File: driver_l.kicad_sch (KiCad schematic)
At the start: 0 parts

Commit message: Simplified sheet tree; fixed all labels
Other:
- company: (none) -> CC0-1.0 License
- title: (none) -> Left Driver
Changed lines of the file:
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@@
 	(generator_version "8.0")
 	(paper "A4")
+	(title_block
+		(title "Left Driver")
+		(date "2025-02-10")
+		(rev "INDEV")
+		(company "CC0-1.0 License")
+	)
 )

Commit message: Update driver motor scheme
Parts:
- added C10, C11, C12, C13, C14, C15, C16, C17, C20: ~, symbol Device:C
- added M1: Motor_DC, symbol Motor:Motor_DC
- added Q2: PNP, symbol Simulation_SPICE:PNP
- added Q5, Q6, Q7, Q8: IRFZ48N, symbol Pioneer:IRFZ48N
- added R2, R36, R63: 0, symbol Device:R
- added R26, R34, R38: ~, symbol Device:R
- added R27, R28, R29, R30: 200, symbol Device:R
- added R31, R32: 10.9k, symbol Device:R
- added R33: 5.62k, symbol Device:R
- added R35, R37, R41: 10k, symbol Device:R
- added R39: 27.4k, symbol Device:R
- added R40: 13.3k, symbol Device:R
- added R7, R8: 4.72k, symbol Device:R
- added U12, U6A, U6B: TS922I, symbol Device:Opamp_Dual
- added U13: TD340I, symbol Pioneer:TD340I
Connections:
- new net: C15.1, R34.1, R35.2, U6A.2 (-)
- new net: C15.2, R34.2, R37.1, U6A.1
- new net: C14.1, R39.1, R41.1, U12.8 (V+), U13.2 (VOUT)
- new net: C16.1, R36.1, U6A.3 (+)
- new net: R38.1, R39.2, R40.2, U6B.5 (+)
- new net: Q2.2 (B), R38.2, U6B.7
- new net: Q7.3 (S), R2.1, R26.1, R36.2
- new net: C17.1, R37.2, U6B.6 (-)
- new net: Q6.1 (G), R29.2
- new net: C10.2, Q6.2 (D)
- new net: C11.1, U13.16 (CB2)
- new net: C12.1, U13.19 (CB1)
- new net: R33.2, U13.20 (OSC)
- new net: R41.2, U13.6 (~{STBY})
- new net: Q2.1 (C), R7.2, U13.8 (IN1)
- new net: Q2.3 (E), R8.2, U13.9 (IN2)
- new net: Q8.1 (G), R27.2
- new net: Q7.1 (G), R30.2
- new net: C20.2, Q5.2 (D)
- new net: Q5.1 (G), R28.2
- new net +BATT: C10.1, C13.1, C20.1, U13.1 (VBATT)
- new net G1: U13.10 (CF), U13.4 (CWD)
- new net GND: C13.2, C14.2, C16.2, C17.2, Q8.3 (S), R2.2, R26.2, R31.2, R32.2, R33.1, R35.1, R40.1, R63.1, R63.2, U12.4 (V-), U13.11 (GND)
- new net H1: R29.1, U13.18 (H1)
- new net H2: R28.1, U13.15 (H2)
- new net L1: R27.1, R32.1, U13.12 (L1)
- new net L2: R30.1, R31.1, U13.13 (L2)
- new net Right_C1: R7.1
- new net Right_C2: R8.1
- new net S1: C12.2, M1.1 (+), Q8.2 (D), U13.17 (S1)
- new net S2: C11.2, M1.2 (-), Q7.2 (D), U13.14 (S2)
- no-connect marks 0 -> 7

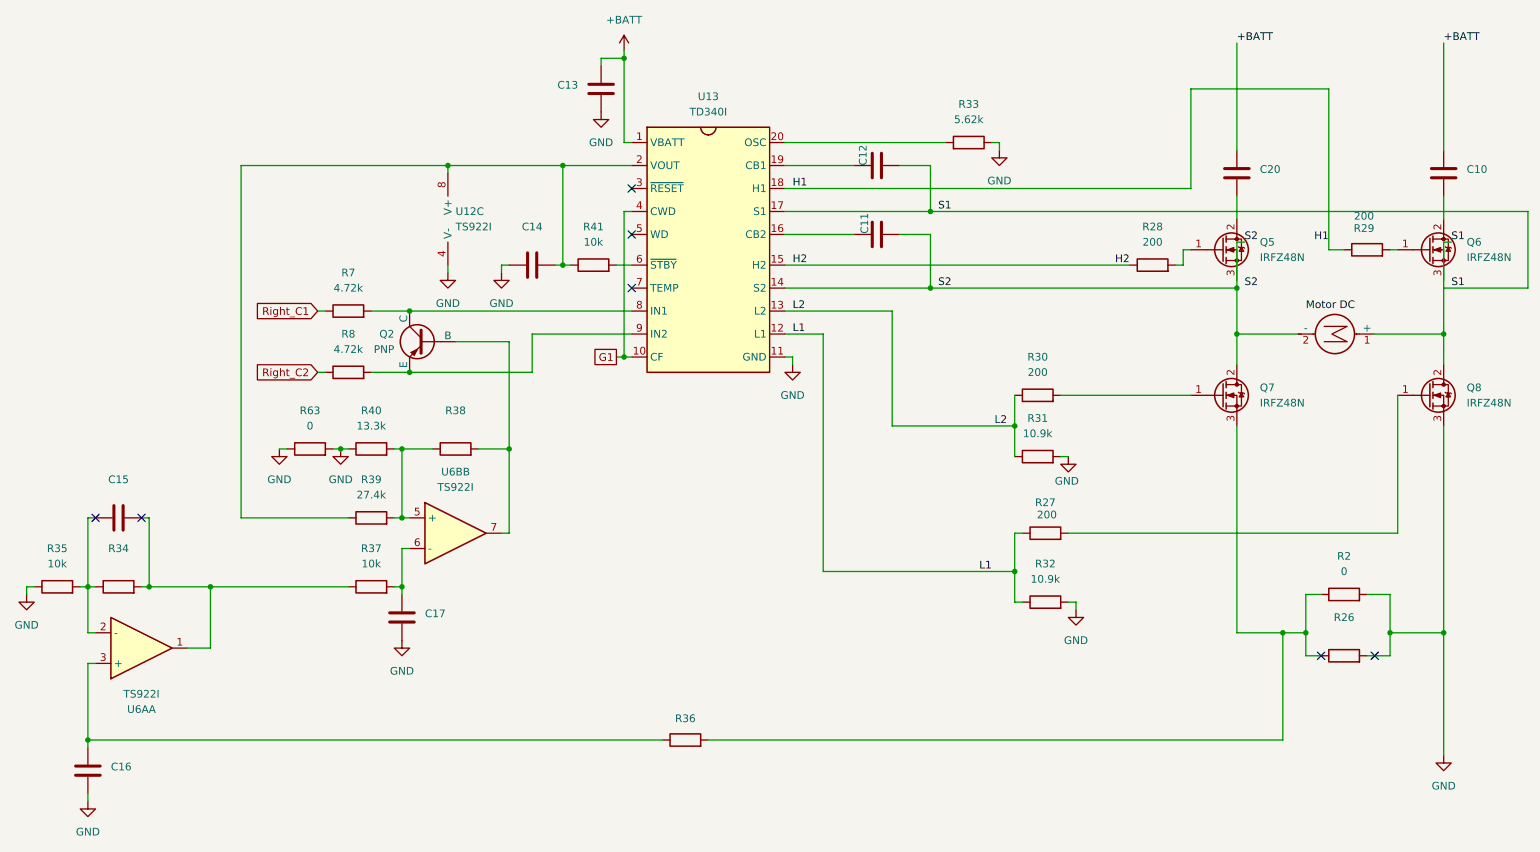
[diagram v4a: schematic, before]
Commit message: Upgrad left driver scheme
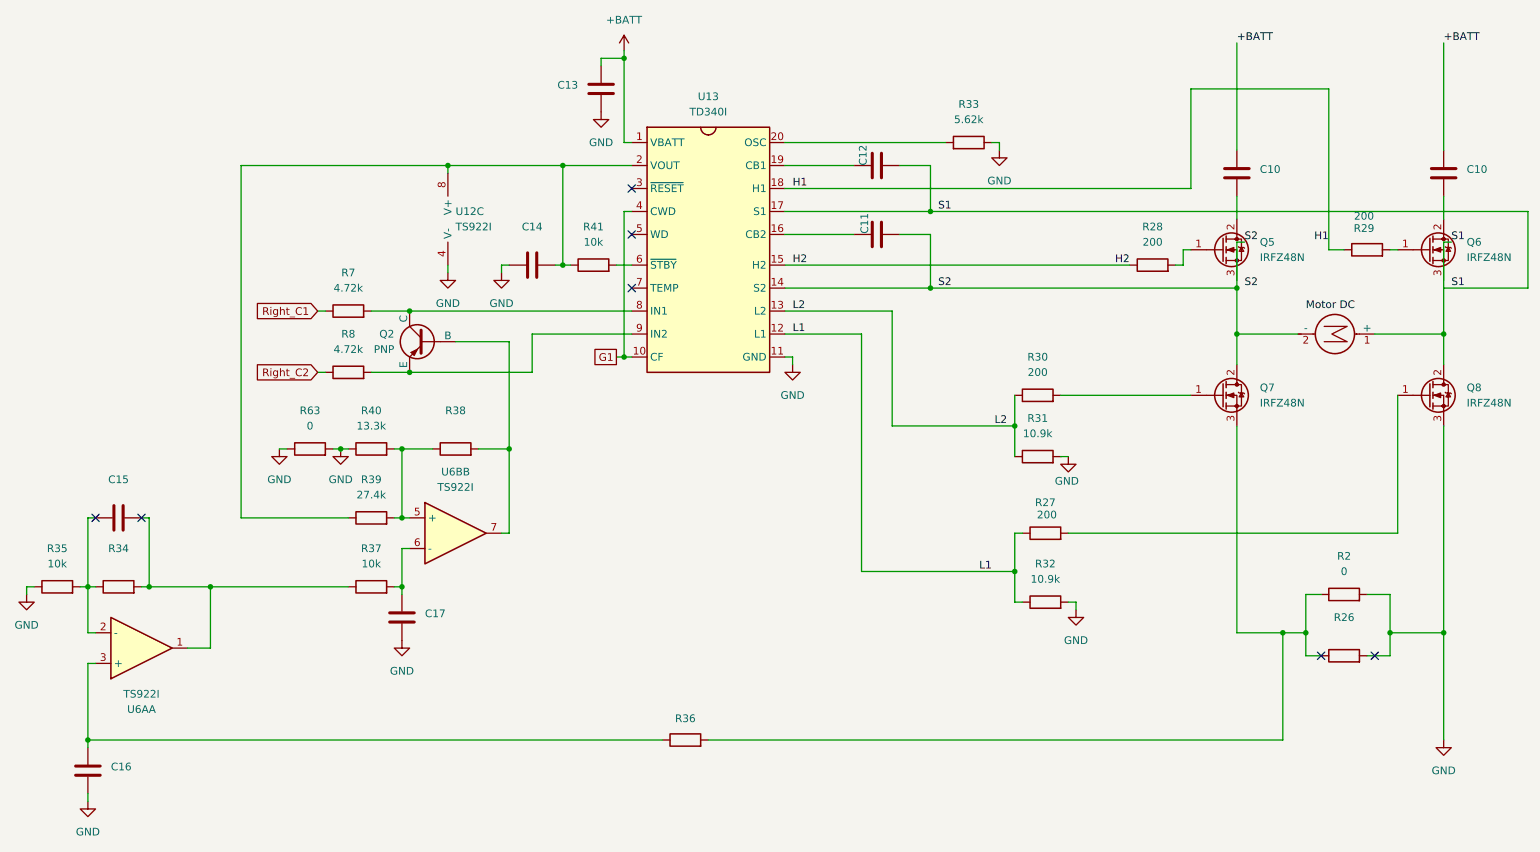
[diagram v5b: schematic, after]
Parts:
- renumbered C20 to C10
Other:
- title: Left Driver -> Right Driver
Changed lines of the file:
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@@
 	(paper "A4")
 	(title_block
-		(title "Left Driver")
+		(title "Right Driver")
 		(date "2025-02-20")
 		(rev "INDEV")
@@
 	(wire
 		(pts
-			(xy 165.1 118.11) (xy 196.85 118.11)
+			(xy 171.45 118.11) (xy 196.85 118.11)
 		)
 		(stroke
@@
 	(wire
 		(pts
-			(xy 165.1 78.74) (xy 158.75 78.74)
+			(xy 171.45 78.74) (xy 158.75 78.74)
 		)
 		(stroke
@@
 	(wire
 		(pts
-			(xy 267.97 128.27) (xy 267.97 148.59)
+			(xy 267.97 128.27) (xy 267.97 146.05)
 		)
 		(stroke
@@
 	(wire
 		(pts
-			(xy 165.1 78.74) (xy 165.1 118.11)
+			(xy 171.45 78.74) (xy 171.45 118.11)
 		)
 		(stroke
@@
 	(symbol
 		(lib_id "power:GND")
-		(at 267.97 148.59 0)
+		(at 267.97 146.05 0)
 		(unit 1)
 		(exclude_from_sim no)
@@
 		(fields_autoplaced yes)
 		(property "Reference" "#PWR075"
-			(at 267.97 154.94 0)
+			(at 267.97 152.4 0)
 			(effects
 				(font
@@
 		)
 		(property "Value" "GND"
-			(at 267.97 153.67 0)
+			(at 267.97 151.13 0)
 			(effects
 				(font
@@
 		)
 		(property "Footprint" ""
-			(at 267.97 148.59 0)
+			(at 267.97 146.05 0)
 			(effects
 				(font
@@
 		)
 		(property "Datasheet" ""
-			(at 267.97 148.59 0)
+			(at 267.97 146.05 0)
 			(effects
 				(font
@@
 		)
 		(property "Description" "Power symbol creates a global label with name \"GND\" , ground"
-			(at 267.97 148.59 0)
+			(at 267.97 146.05 0)
 			(effects
 				(font
@@
 		(dnp no)
 		(fields_autoplaced yes)
-		(property "Reference" "C20"
+		(property "Reference" "C10"
 			(at 237.49 51.4349 0)
 			(effects
@@
 			(project "p3dx"
 				(path "/d0830b7c-35c9-4293-a1d2-d544311c2c60/4a922283-64e3-444c-94b3-c33ac63de612"
-					(reference "C20")
+					(reference "C10")
 					(unit 1)
 				)

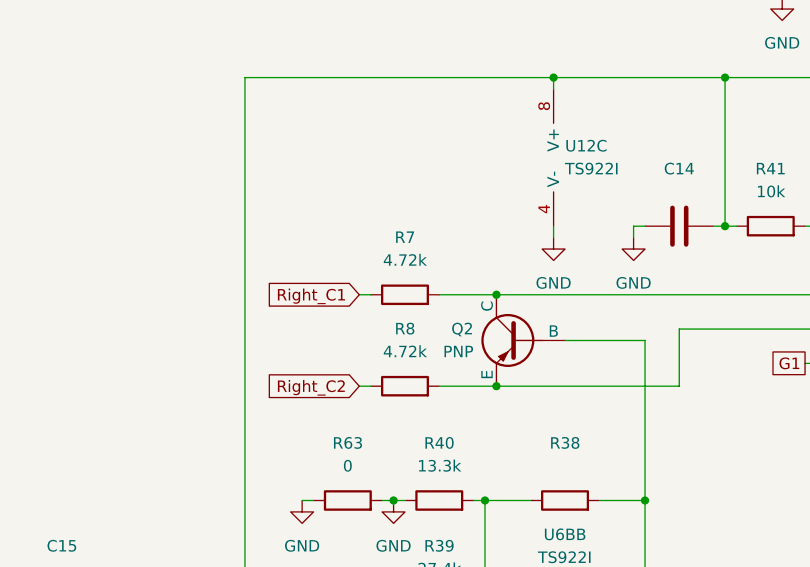
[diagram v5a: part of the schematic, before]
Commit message: Update J28 pin name
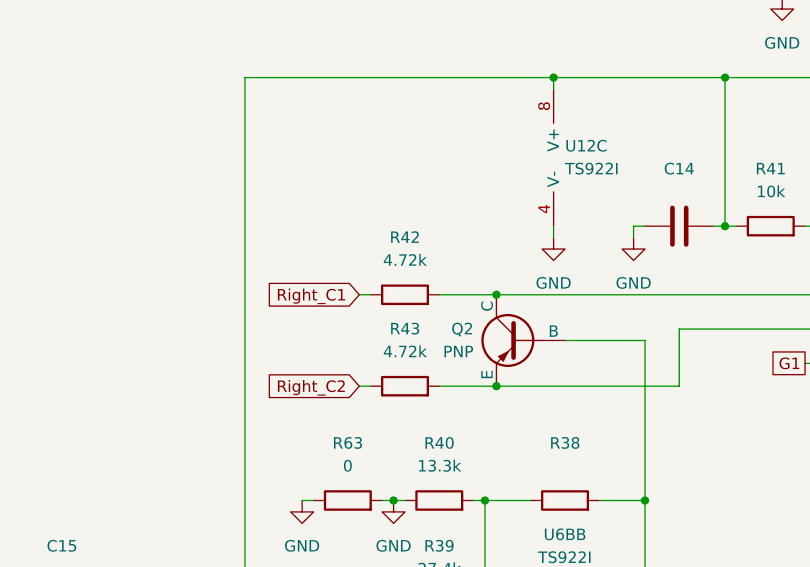
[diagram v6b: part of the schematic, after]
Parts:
- renumbered R7 to R42, R8 to R43
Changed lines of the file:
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@@
 		(dnp no)
 		(fields_autoplaced yes)
-		(property "Reference" "R8"
+		(property "Reference" "R43"
 			(at 86.36 78.74 90)
 			(effects
@@
 			(project "p3dx"
 				(path "/d0830b7c-35c9-4293-a1d2-d544311c2c60/4a922283-64e3-444c-94b3-c33ac63de612"
-					(reference "R8")
+					(reference "R43")
 					(unit 1)
 				)
@@
 		(dnp no)
 		(fields_autoplaced yes)
-		(property "Reference" "R7"
+		(property "Reference" "R42"
 			(at 86.36 68.58 90)
 			(effects
@@
 			(project "p3dx"
 				(path "/d0830b7c-35c9-4293-a1d2-d544311c2c60/4a922283-64e3-444c-94b3-c33ac63de612"
-					(reference "R7")
+					(reference "R42")
 					(unit 1)
 				)

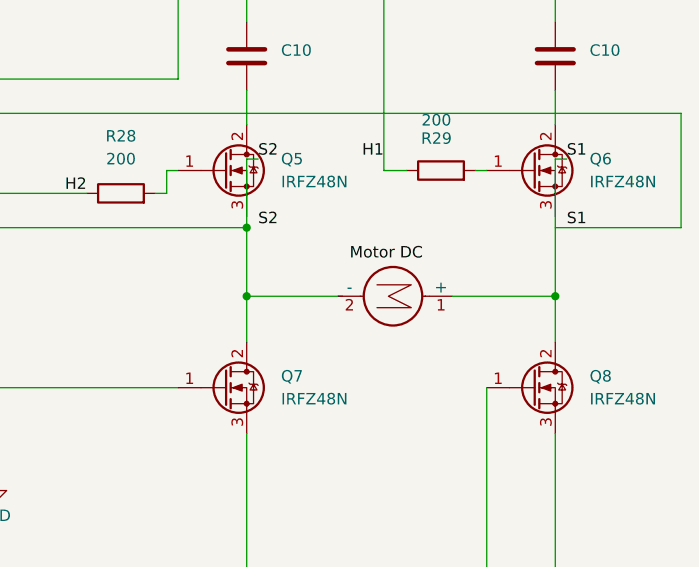
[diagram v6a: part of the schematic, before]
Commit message: Update driver scheme and added User Control Panel scheme
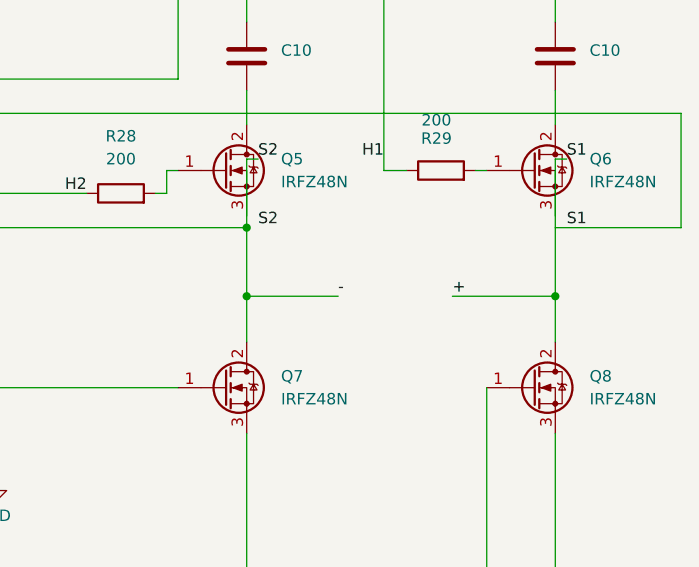
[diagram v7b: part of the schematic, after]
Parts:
- removed M1: Motor_DC, symbol Motor:Motor_DC
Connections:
- net S1 renamed +
- net S2 renamed -
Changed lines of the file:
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@@
-		)
-	)
-	(label "Motor DC"
-		(at 245.11 74.93 0)
-		(effects
-			(font
-				(size 1.27 1.27)
-			)
-			(justify left bottom)
 		)
 	)
@@
 	(label "H1"
 		(at 160.02 54.61 0)
+		(effects
+			(font
+				(size 1.27 1.27)
+			)
+			(justify left bottom)
+		)
+	)
+	(label "-"
+		(at 243.84 78.74 0)
+		(effects
+			(font
+				(size 1.27 1.27)
+			)
+			(justify left bottom)
+		)
+	)
+	(label "+"
+		(at 256.54 78.74 0)
 		(effects
 			(font
@@
 					(unit 1)
 				)
-			)
-		)
-	)
-	(symbol
-		(lib_id "Motor:Motor_DC")
-		(at 251.46 78.74 270)
-		(unit 1)
-		(exclude_from_sim no)
-		(in_bom yes)
-		(on_board yes)
-		(dnp no)
-		(property "Reference" "M1"
-			(at 250.1901 83.82 0)
-			(effects
-				(font
-					(size 1.27 1.27)
-				)
-				(justify left)
-				(hide yes)
-			)
-		)
-		(property "Value" "Motor_DC"
-			(at 244.856 70.612 0)
-			(effects
-				(font
-					(size 1.27 1.27)
-				)
-				(justify left)
-				(hide yes)
-			)
-		)
-		(property "Footprint" ""
-			(at 249.174 78.74 0)
-			(effects
-				(font
-					(size 1.27 1.27)
-				)
-				(hide yes)
-			)
-		)
-		(property "Datasheet" "~"
-			(at 249.174 78.74 0)
-			(effects
-				(font
-					(size 1.27 1.27)
-				)
-				(hide yes)
-			)
-		)
-		(property "Description" "DC Motor"
-			(at 251.46 78.74 0)
-			(effects
-				(font
-					(size 1.27 1.27)
-				)
-				(hide yes)
-			)
-		)
-		(pin "1"
-		)
-		(pin "2"
-		)
-		(instances
-			(project ""
-				(path "/d0830b7c-35c9-4293-a1d2-d544311c2c60/4a922283-64e3-444c-94b3-c33ac63de612"
-					(reference "M1")
-					(unit 1)
-				)
